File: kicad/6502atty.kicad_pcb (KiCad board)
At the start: 2 copper layers, 100 x 100 mm, 104 parts, among them J1 Conn_01x04_Pin, J10 Conn_01x04_Pin, J11 Conn_01x03_Pin, J12 Conn_01x02_Pin, J2 Conn_01x02_Pin, J3 Conn_02x03_Odd_Even, J4 Conn_01x03_Pin, J5 Conn_01x06_Pin, J6 Conn_01x04_Pin, J7 Conn_01x10_Pin, J9 Conn_01x10_Pin, SW1 SW_Push, U1 ATmega164P-20P, U10 74LS08, U11 74LS138, U12 74LS574, U2 74LS112, U3 W65C02SxP, U4 74LS574, U5 74HC245, U6 27C128, U7 KM62256CLP, U8 74LS00, U9 74LS00, Y1 18.432MHz

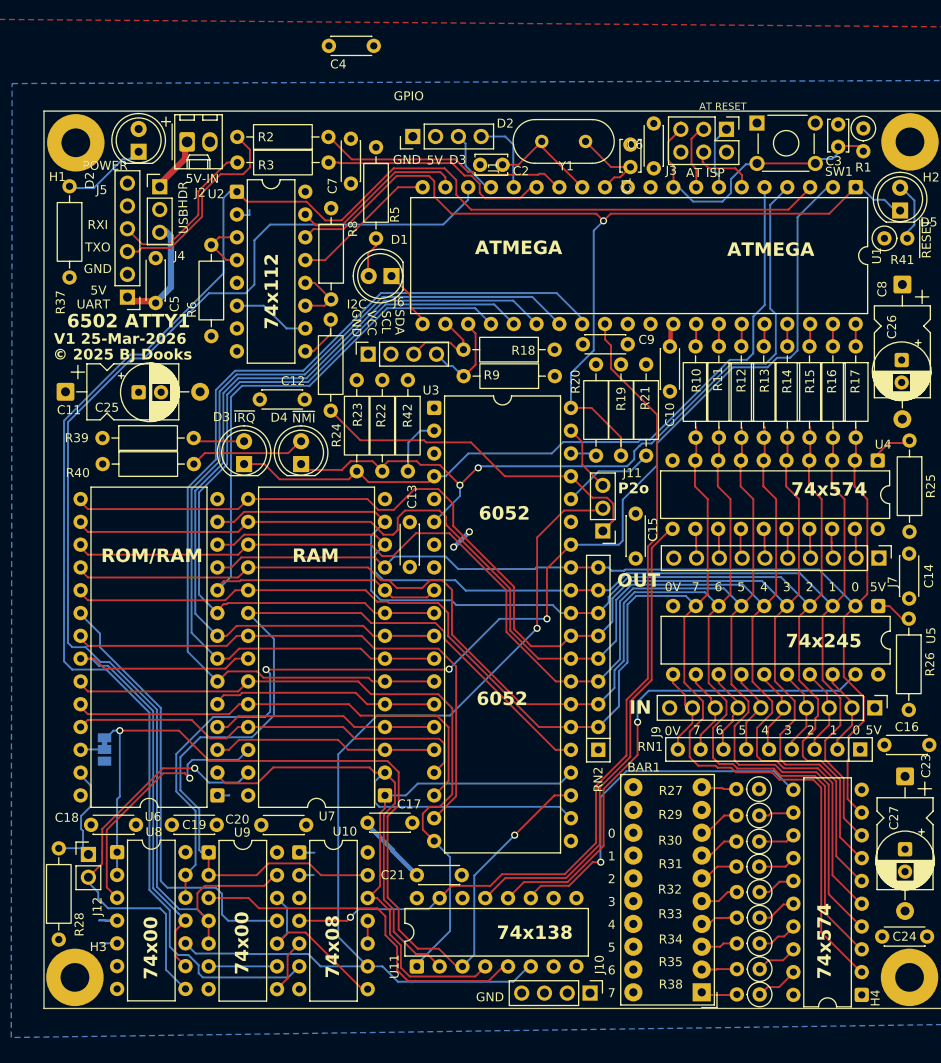
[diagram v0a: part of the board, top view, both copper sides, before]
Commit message: update to kicad10, v1_r3 release
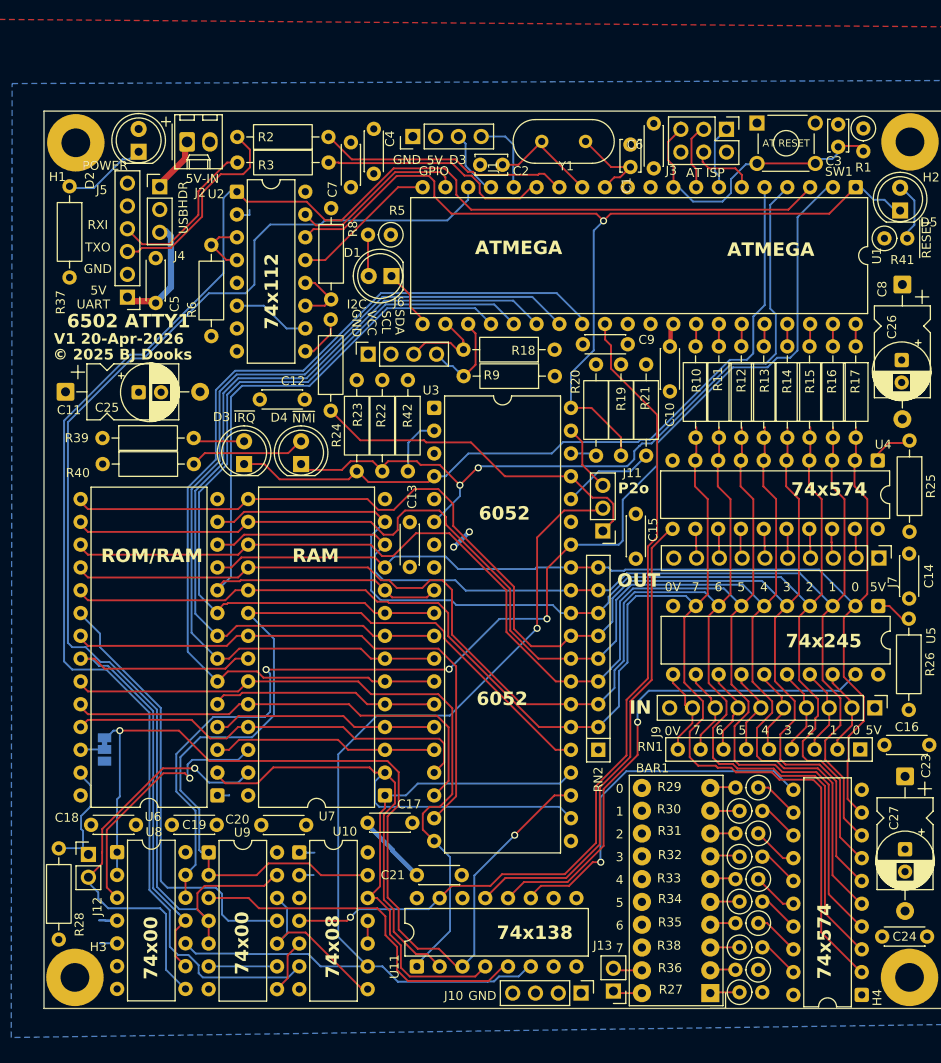
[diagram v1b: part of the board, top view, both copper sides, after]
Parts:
- added J13: Conn_01x02_Pin, Connector_PinHeader_2.54mm:PinHeader_1x02_P2.54mm_Vertical, F.Cu at (63.5, 99.7)
- added R36: 680R, Resistor_THT:R_Axial_DIN0207_L6.3mm_D2.5mm_P2.54mm_Vertical, F.Cu at (79.6, 97.3)
- R5: footprint Resistor_THT:R_Axial_DIN0207_L6.3mm_D2.5mm_P10.16mm_Horizontal -> Resistor_THT:R_Axial_DIN0207_L6.3mm_D2.5mm_P2.54mm_Vertical
- moved R27 22.7 mm to (77.6, 99.8), turned to 0 degrees
- moved R5 9.89 mm to (38.7, 15.4), turned to 180 degrees
- moved C4 9.25 mm to (36.8, 3.60), turned to -90 degrees
- moved R38 5.71 mm to (77.6, 94.8), turned to 0 degrees
- moved R34 5.18 mm to (77.6, 89.7), turned to 0 degrees
- moved R35 5.13 mm to (79.6, 92.1)
- moved R32 4.53 mm to (77.6, 84.7), turned to 0 degrees
- moved R33 4.30 mm to (79.6, 87.2)
- moved R30 4.05 mm to (77.6, 79.6), turned to 0 degrees
- moved R31 3.71 mm to (79.6, 82.1)
- moved R29 3.11 mm to (79.6, 77.0)
- moved J10 1.00 mm to (59.9, 99.9)
- moved BAR1 0.96 mm to (74.3, 99.9)
- moved C7 0.40 mm to (34.2, 10.1)
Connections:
- BAR1 pad 19: GND -> Net-(BAR1B-K)
- BAR1 pad 20: GND -> Net-(BAR1A-K)
- BAR1 pad 9: unconnected-(BAR1I-A-Pad9) -> Net-(BAR1I-A)
- R27 pad 1: VCC -> Net-(BAR1A-A)
- R27 pad 2: Net-(BAR1J-A) -> VCC
- R29 pad 2: Net-(BAR1H-A) -> Net-(BAR1J-A)
- R30 pad 1: /IO/DQ1 -> Net-(BAR1I-A)
- R30 pad 2: Net-(BAR1G-A) -> /IO/DQ1
- R31 pad 2: Net-(BAR1F-A) -> Net-(BAR1H-A)
- R32 pad 1: /IO/DQ3 -> Net-(BAR1G-A)
- R32 pad 2: Net-(BAR1E-A) -> /IO/DQ3
- R33 pad 2: Net-(BAR1D-A) -> Net-(BAR1F-A)
- R34 pad 1: /IO/DQ5 -> Net-(BAR1E-A)
- R34 pad 2: Net-(BAR1C-A) -> /IO/DQ5
- R35 pad 2: Net-(BAR1B-A) -> Net-(BAR1D-A)
- R38 pad 1: /IO/DQ7 -> Net-(BAR1C-A)
- R38 pad 2: Net-(BAR1A-A) -> /IO/DQ7
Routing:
- net Net-(BAR1A-K): track 0.00 -> 3.27 mm
- net Net-(BAR1B-K): track 0.00 -> 3.27 mm
- net Net-(BAR1I-A): track 0.00 -> 3.26 mm
- net Net-(D1-A): track 4.59 -> 7.16 mm
- net Net-(BAR1H-A): track 4.67 -> 2.81 mm
- net Net-(BAR1D-A): track 4.45 -> 2.88 mm
- net Net-(BAR1F-A): track 4.41 -> 2.88 mm
- net Net-(BAR1G-A): track 4.52 -> 3.34 mm
- net /IO/DQ0: track 3.94 -> 5.06 mm
- net Net-(BAR1B-A): track 3.97 -> 2.85 mm
- net Net-(BAR1E-A): track 4.33 -> 3.27 mm
- net /IO/DQ2: track 4.24 -> 5.05 mm
- net Net-(BAR1C-A): track 4.06 -> 3.26 mm
- net Net-(BAR1A-A): track 4.07 -> 3.30 mm
- net /IO/DQ7: track 5.20 -> 4.60 mm
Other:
- board text added: "V1 20-Apr-2026"
- board text added: "V1 R3 20-Apr-2026"
- board text removed: "D2"
- board text removed: "V1 25-Mar-2026"

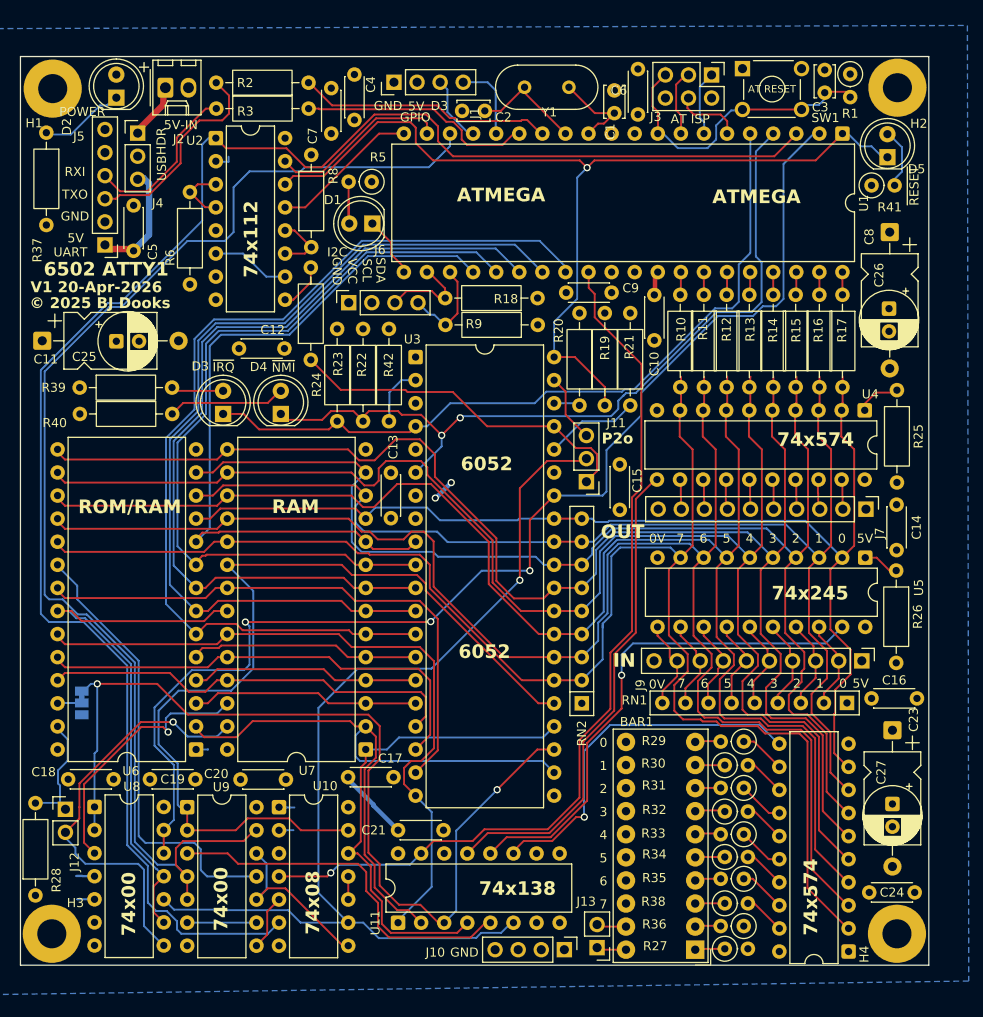
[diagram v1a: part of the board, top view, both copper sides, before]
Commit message: updated to use 74x574 for input, then drc fixes
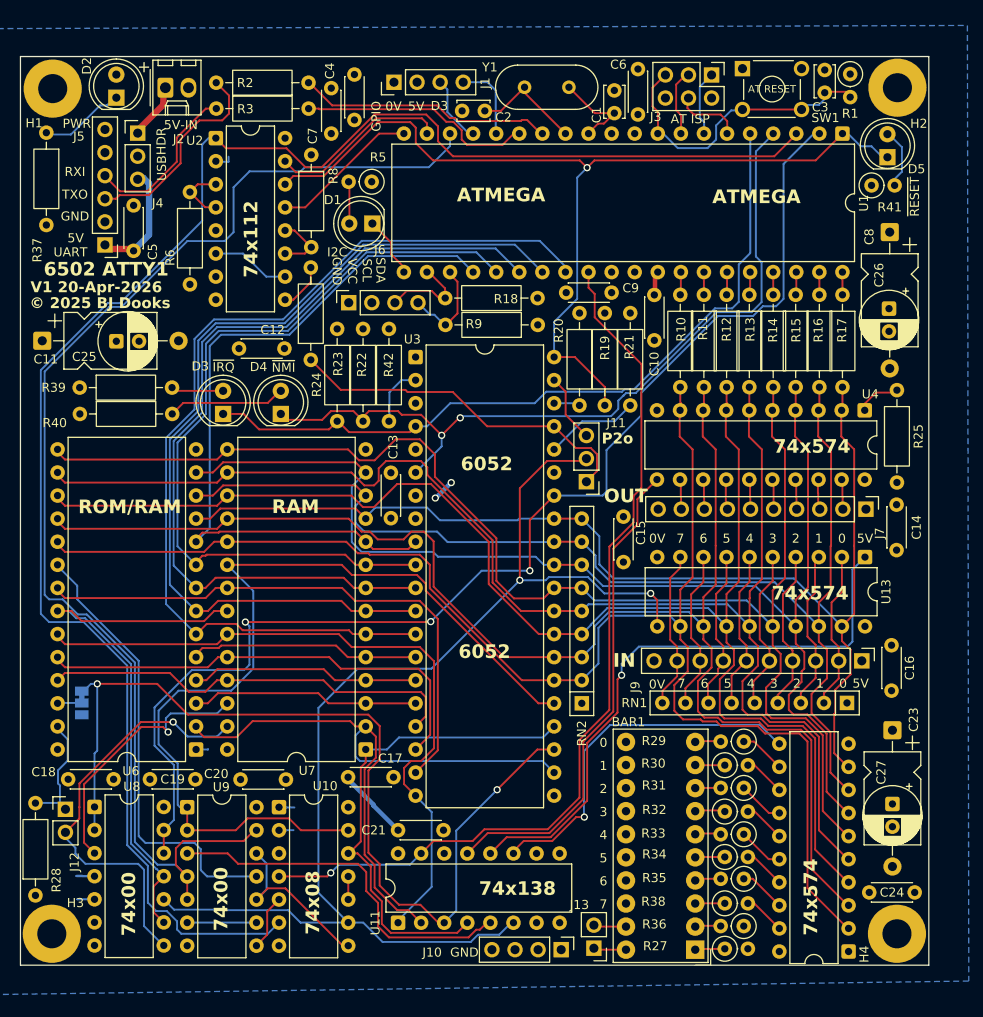
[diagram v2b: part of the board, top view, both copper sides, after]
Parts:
- removed R26: 4K7, Resistor_THT:R_Axial_DIN0207_L6.3mm_D2.5mm_P10.16mm_Horizontal
- removed U5: 74HC245, Package_DIP:DIP-20_W7.62mm
- added U13: 74LS574, Package_DIP:DIP-20_W7.62mm, F.Cu at (93.0, 56.7)
- moved C16 6.25 mm to (95.9, 66.4), turned to -90 degrees
- moved C15 5.76 mm to (66.4, 52.2)
- moved REF** 0.65 mm to (85.7, 17.9)
- moved J13 0.36 mm to (63.1, 99.7)
- moved J10 0.35 mm to (59.5, 99.9)
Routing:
- net /PHI2: track 112.7 -> 132.3 mm, vias 1 -> 2
- net /~{IO_IN}: track 56.2 -> 66.0 mm
- net /D7: track 168.9 -> 160.4 mm
- net /IO/IN6: track 9.94 -> 18.3 mm
- net /IO/IN3: track 10.6 -> 18.8 mm
- net /D5: track 164.1 -> 156.0 mm
- net /D6: track 166.6 -> 158.6 mm
- net /IO/IN1: track 10.2 -> 18.2 mm
- net /IO/IN0: track 10.6 -> 18.6 mm
- net /IO/IN4: track 10.4 -> 18.4 mm
- net /IO/IN5: track 10.0 -> 17.9 mm
- net /IO/IN2: track 9.94 -> 17.7 mm
- net /IO/IN7: track 10.1 -> 17.8 mm
- net /D4: track 161.5 -> 154.8 mm
- net /D3: track 158.4 -> 152.6 mm
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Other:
- board text added: "PWR"
- board text removed: "74x245"
- board text removed: "POWER"

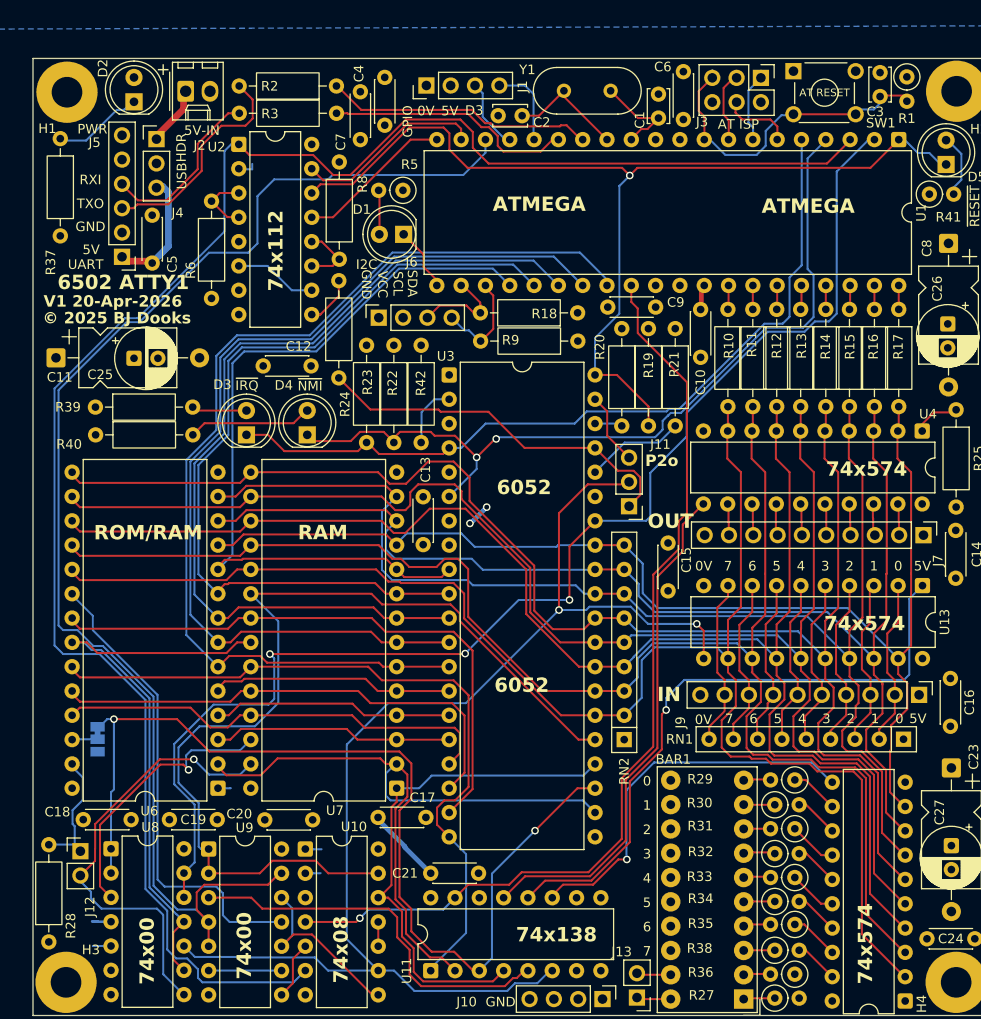
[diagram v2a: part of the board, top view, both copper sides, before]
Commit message: pcb: updated silkscreen bits
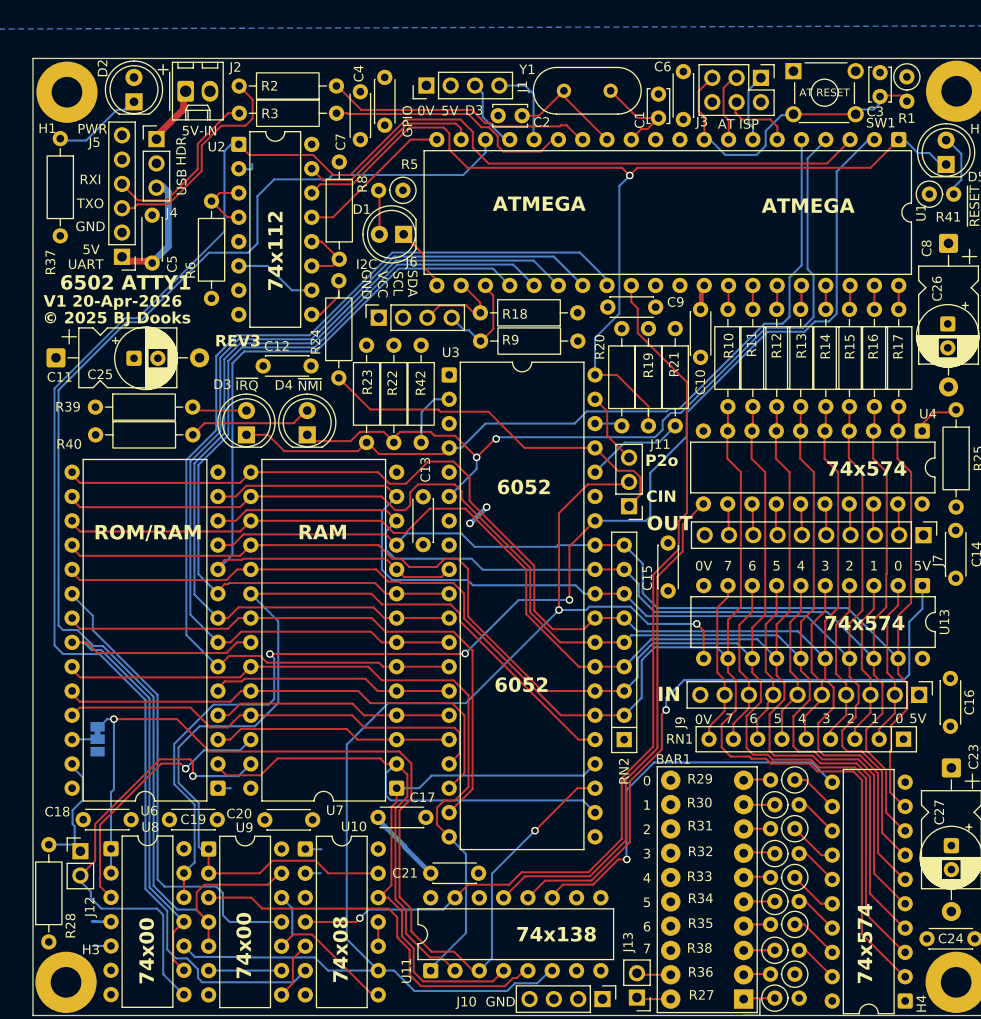
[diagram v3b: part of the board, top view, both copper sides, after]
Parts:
- moved REF** 51.3 mm to (51.2, 55.9)
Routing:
- net /~{A13}: track 29.2 -> 27.9 mm
- net /R~{W}ph: track 47.0 -> 48.0 mm
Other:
- board text added: "CIN"
- board text added: "REV3"

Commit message: kicad: v1_rev3 production
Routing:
- net /Atmel Controller/PD3: track 7.42 -> 13.4 mm
- net GND: track 12.6 -> 14.2 mm
- net /D0: track 124.8 -> 125.7 mm
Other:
- board text added: "LED BAR"
- board text added: "ROM-A13 SEL"
- board text added: "XTAL"
